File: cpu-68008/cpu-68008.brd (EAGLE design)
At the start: 96.8 x 100 mm, 65 parts, among them IC1 68008, IC11 NE555, IC2 AS6C4008, IC3 39SF010, IC4 DS1244Y, IC5 XR68C681, Q1 8MHz, Q3 3.6864 MHz

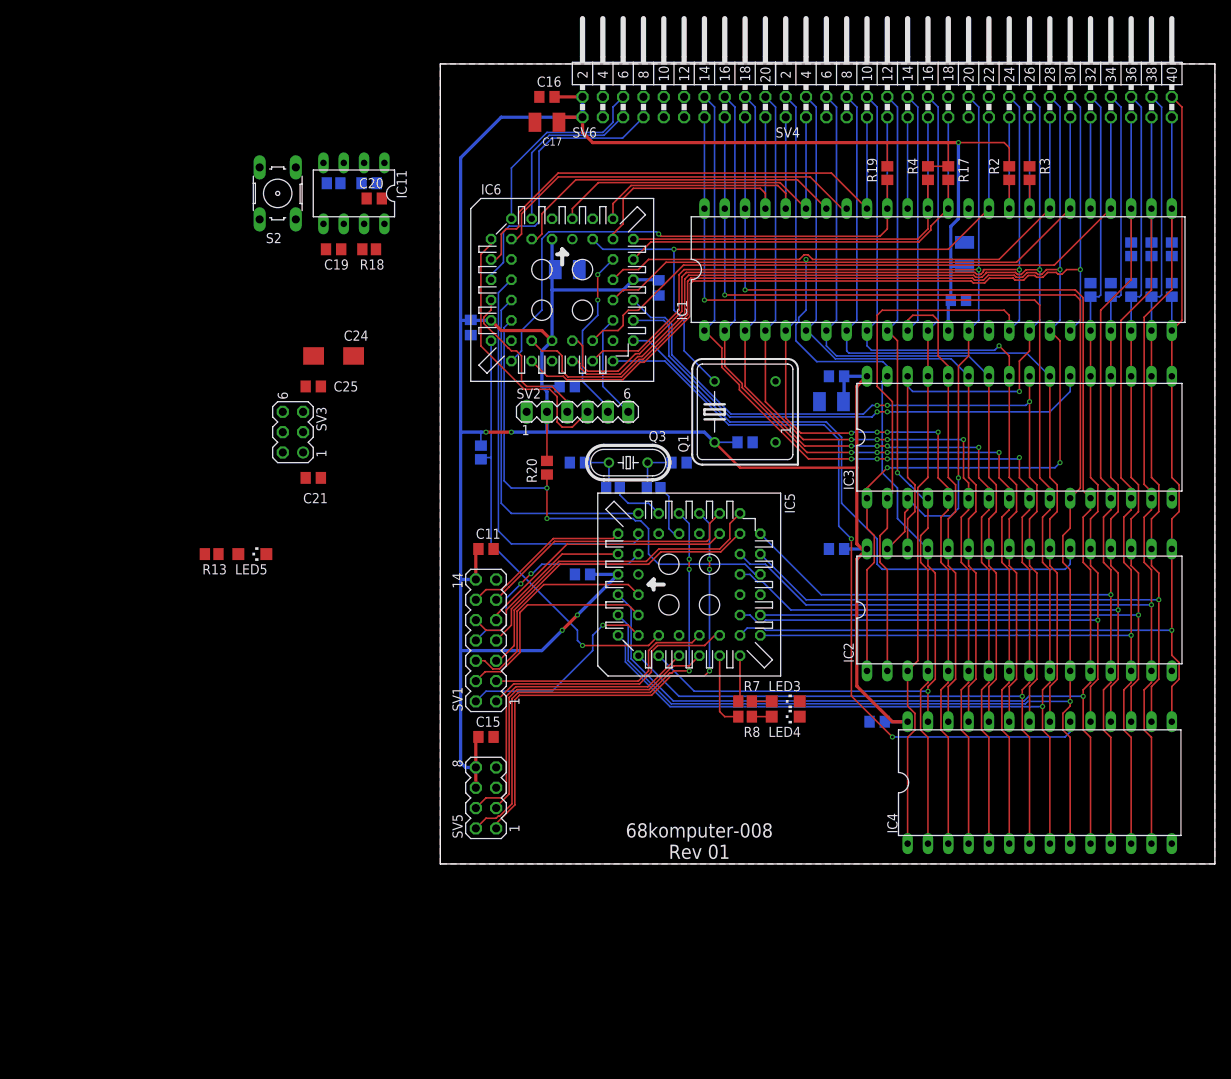
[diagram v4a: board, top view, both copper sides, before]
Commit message: finish routng
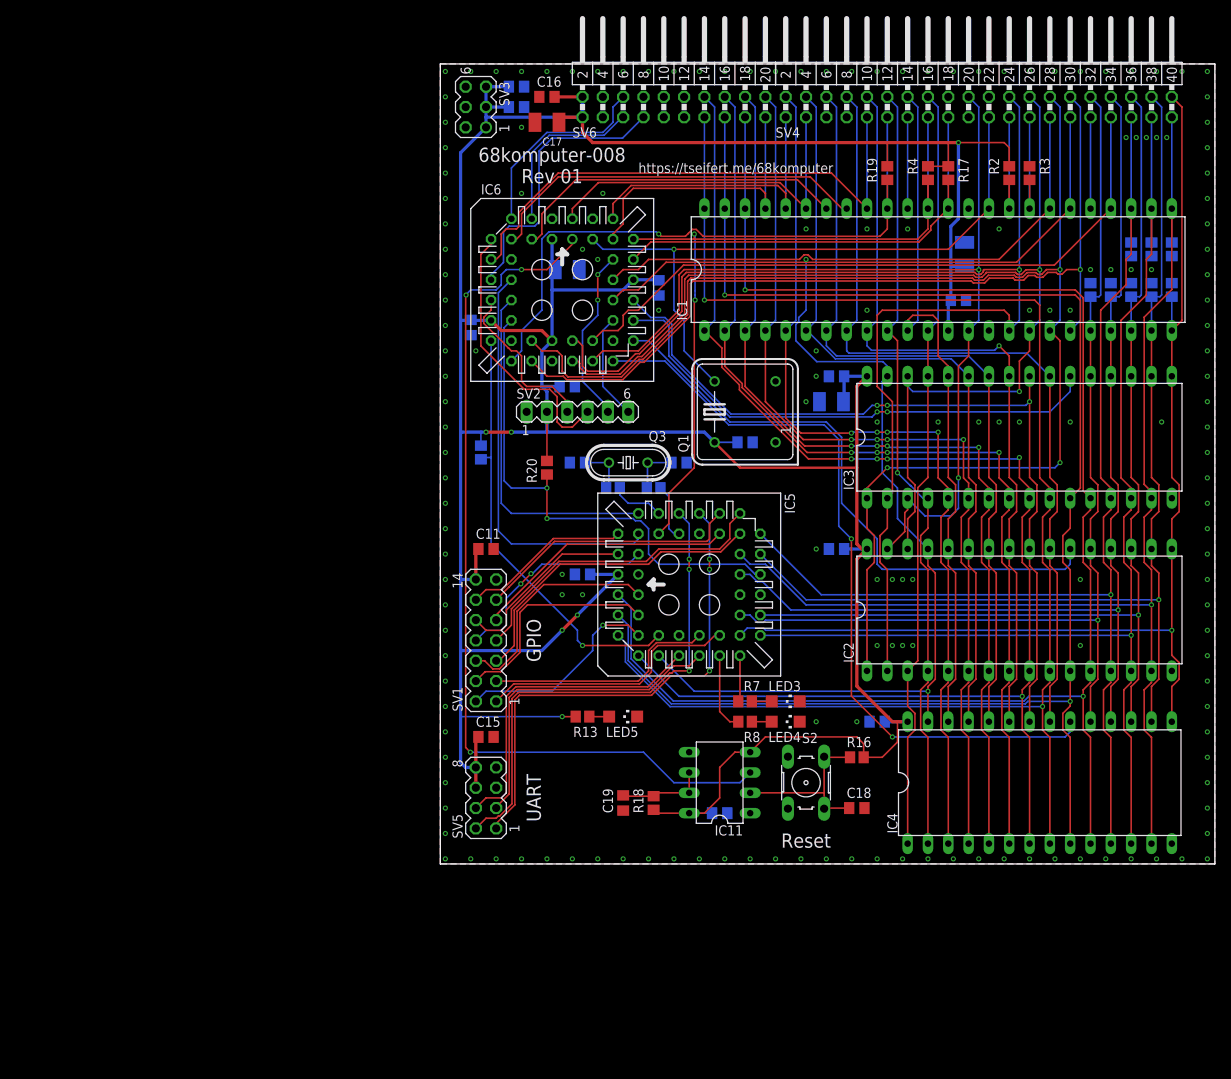
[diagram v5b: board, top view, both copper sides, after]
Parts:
- removed C24: 47µF, rcl:CT6032
- moved C18 99.1 mm to (52.1, 6.99), flipped to the top, turned to 0 degrees
- moved S2 98.9 mm to (45.7, 10.2), turned to 270 degrees
- moved R16 97.1 mm to (52.1, 13.3), flipped to the top
- moved C20 88.1 mm to (34.9, 6.35), flipped to the bottom
- moved IC11 86.7 mm to (34.9, 10.2), turned to 90 degrees
- moved C19 78.1 mm to (22.9, 7.62), turned to 270 degrees
- moved R18 77.8 mm to (26.7, 7.62), turned to 90 degrees
- moved C21 52.9 mm to (9.53, 94.6), flipped to the bottom, turned to 180 degrees
- moved LED5 50.6 mm to (22.9, 18.4)
- moved R13 50.6 mm to (17.8, 18.4)
- moved SV3 46.6 mm to (4.45, 94.6)
- moved C25 45.3 mm to (9.53, 97.2), flipped to the bottom, turned to 180 degrees
- moved LED4 0.63 mm to (43.2, 17.8)
- moved R8 0.63 mm to (38.1, 17.8)
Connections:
- net +5V: no longer C24.+
- net GND: no longer C24.-
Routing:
- net RESET: track 0.00 -> 111.8 mm, vias 0 -> 3
- net +5V: track 413.4 -> 483.5 mm, vias 5 -> 6
- net !RESET: track 54.9 -> 94.9 mm, vias 0 -> 2
- net N$1: track 0.00 -> 22.2 mm
- net N$12: track 0.00 -> 11.0 mm
- net N$4: track 0.00 -> 2.48 mm
- net !VPA: track 78.6 -> 79.3 mm
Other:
- board text added: "GPIO"
- board text added: "Reset"
- board text added: "UART"
- board text added: "https://tseifert.me/68komputer"

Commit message: a few routing improvements
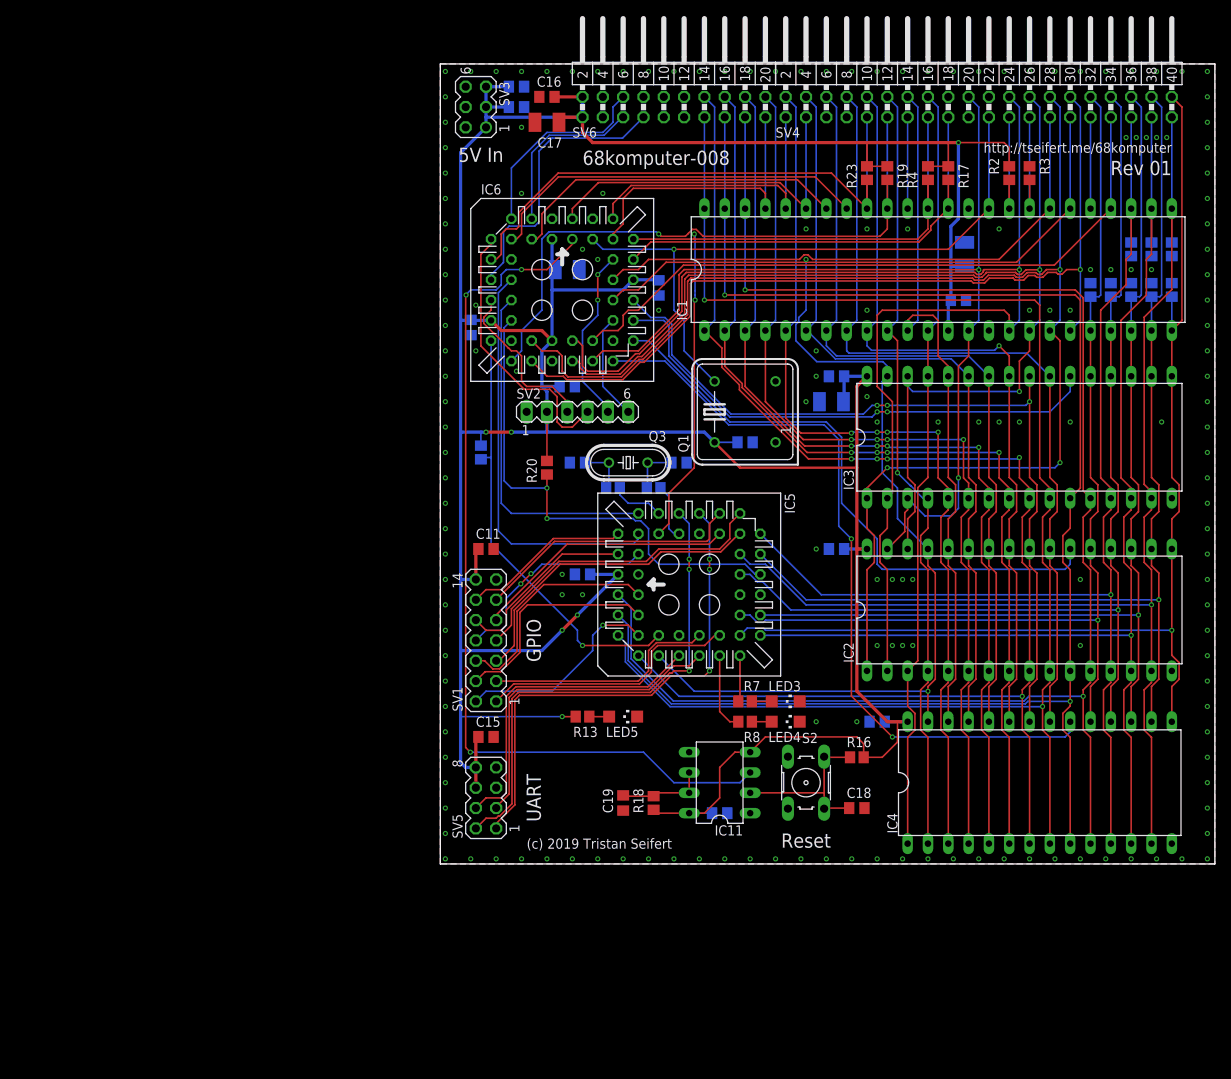
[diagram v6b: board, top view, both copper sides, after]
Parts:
- added R23: 10k, rcl:R2012
- IC6: value (none) -> ATF1504AS
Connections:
- net !BERR: now also R23.2
- net +5V: now also R23.1
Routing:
- net !BERR: track 67.3 -> 70.9 mm
- net +5V: track 483.5 -> 486.3 mm
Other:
- board text added: "(c) 2019 Tristan Seifert"
- board text added: "5V In"
- board text added: "68komputer-008"
- board text added: "Rev 01"
- board text added: "http://tseifert.me/68komputer"
- board text removed: "68komputer-008 Rev 01"
- board text removed: "https://tseifert.me/68komputer"

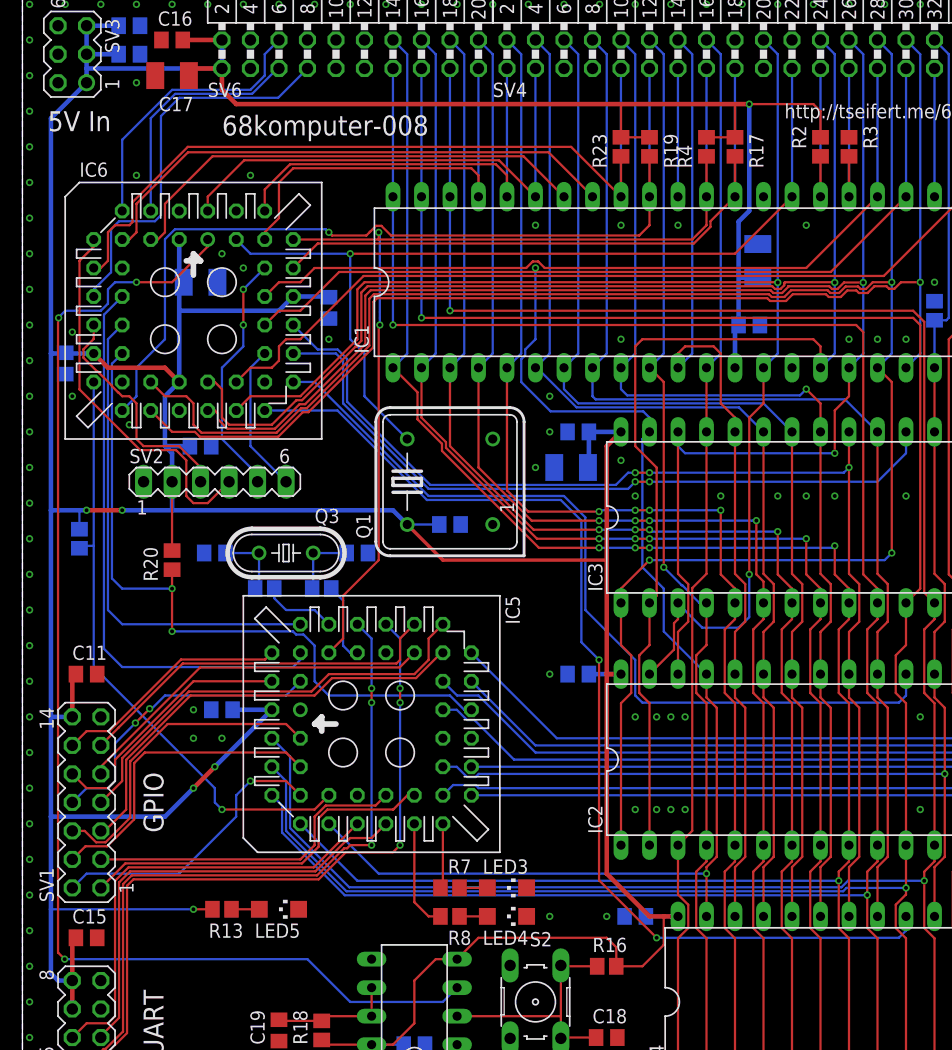
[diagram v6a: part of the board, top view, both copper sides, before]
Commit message: replaced CPLD with PLDs
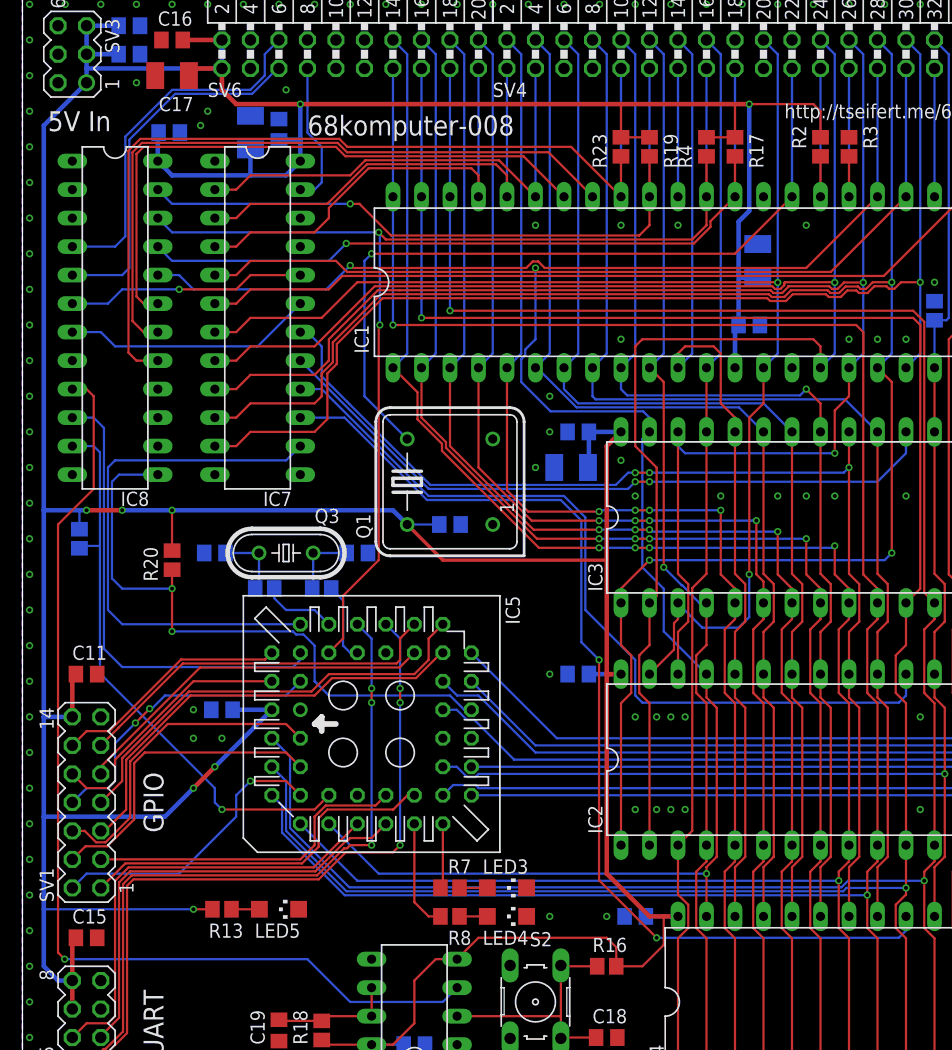
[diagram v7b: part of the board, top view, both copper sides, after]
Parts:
- removed C22: 100nF, rcl:C0805
- removed IC6: ATF1504AS, 68komputer:PLCC-S44
- removed SV2: (no value), con-lstb:MA06-1
- added IC7, IC8: (no value), 68komputer:DIL24S
- moved C9 28.2 mm to (22.9, 87.9), turned to 90 degrees
- moved C12 21.1 mm to (13.1, 87.6), turned to 180 degrees
- moved C14 14.1 mm to (20.3, 87.6), turned to 90 degrees
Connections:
- removed net CPLD_TCK: IC6.32, SV2.6
- removed net CPLD_TDI: IC6.7, SV2.4
- removed net CPLD_TDO: IC6.38, SV2.5
- removed net CPLD_TMS: IC6.13, SV2.3
- new net !IACK: IC7.19, IC8.7
- new net !REQUIRE_DTACK: IC7.20, IC8.6
- net !68681_CS: now also IC7.14; no longer IC6.14
- net !68681_DTACK: now also IC8.11; no longer IC6.17
- net !68681_IACK: now also IC8.10; no longer IC6.12
- net !68681_IRQ: now also IC8.13; no longer IC6.16
- net !AS: now also IC7.6; no longer IC6.27
- net !BERR: now also IC8.17; no longer IC6.9
- net !BUS_CS: now also IC7.23; no longer IC6.11
- net !BUS_DTACK: now also IC8.4; no longer IC6.6
- net !BUS_IRQ: now also IC8.5; no longer IC6.4
- net !DTACK: now also IC8.20; no longer IC6.36
- net !HALT: now also IC8.21; no longer IC6.37
- net !IPL0/2: now also IC8.19; no longer IC6.5
- net !IPL1: now also IC8.18; no longer IC6.8
- net !OE: now also IC7.18; no longer IC6.33
- net !RAM_CS: now also IC7.16; no longer IC6.29
- net !RESET: now also IC8.22; no longer IC6.39
- net !ROM_CS: now also IC7.17; no longer IC6.31
- net !RTC_CS: now also IC7.15; no longer IC6.28
- net !VPA: now also IC8.23; no longer IC6.18
- net +5V: now also IC7.24, IC8.24; no longer C22.1, IC6.15, IC6.23, IC6.3, IC6.35, SV2.2
- net A15: now also IC7.7; no longer IC6.26
- net A16: now also IC7.8; no longer IC6.25
- net A17: now also IC7.9; no longer IC6.24
- net A18: now also IC7.10; no longer IC6.21
- net A19: now also IC7.11; no longer IC6.20
- net CLK: no longer IC6.43
- net FC0: now also IC7.4; no longer IC6.41
- net FC1: now also IC7.3; no longer IC6.40
- net FC2: now also IC7.2; no longer IC6.44
- net GND: now also IC7.12, IC8.12; no longer C22.2, IC6.10, IC6.22, IC6.30, IC6.42, SV2.1
- net R/!W!: now also IC7.5; no longer IC6.34
- net RESET: now also IC8.9; no longer IC6.1
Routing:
- net CPLD_TDI: track 34.1 -> 0.00 mm
- net +5V: track 486.3 -> 458.4 mm, vias 6 -> 8
- net !IACK: track 0.00 -> 22.4 mm
- net !BUS_CS: track 35.2 -> 12.9 mm
- net CPLD_TDO: track 21.9 -> 0.00 mm, vias 2 -> 0
- net !REQUIRE_DTACK: track 0.00 -> 21.4 mm, vias 0 -> 1
- net CPLD_TMS: track 20.9 -> 0.00 mm
- net RESET: track 111.8 -> 91.0 mm, vias 3 -> 1
- net !VPA: track 79.3 -> 63.5 mm
- net CPLD_TCK: track 13.3 -> 0.00 mm
- net CLK: track 82.2 -> 69.4 mm
- net !IPL1: track 48.3 -> 61.1 mm
- net !HALT: track 57.3 -> 69.6 mm, vias 0 -> 1
- net !RESET: track 94.9 -> 107.2 mm
- net !IPL0/2: track 42.9 -> 55.1 mm
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
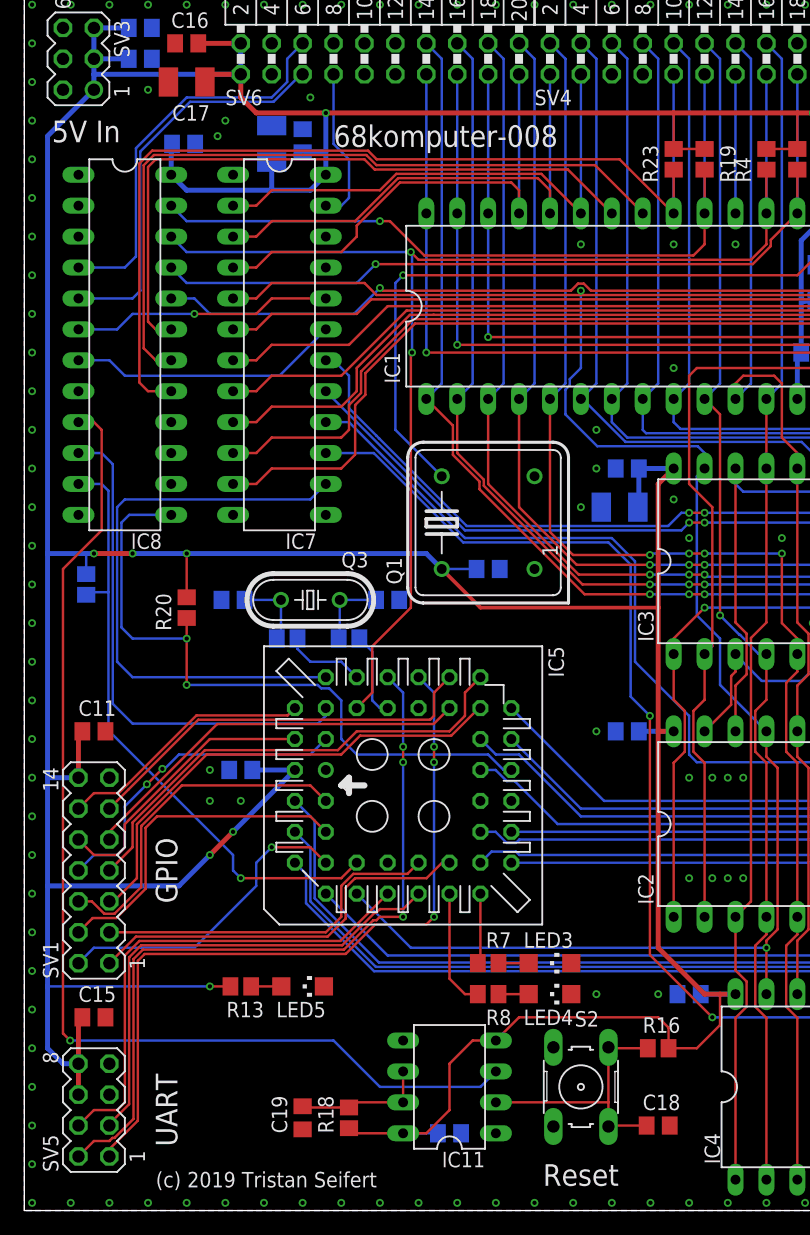
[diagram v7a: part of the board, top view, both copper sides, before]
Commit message: added bus error timeout circuit
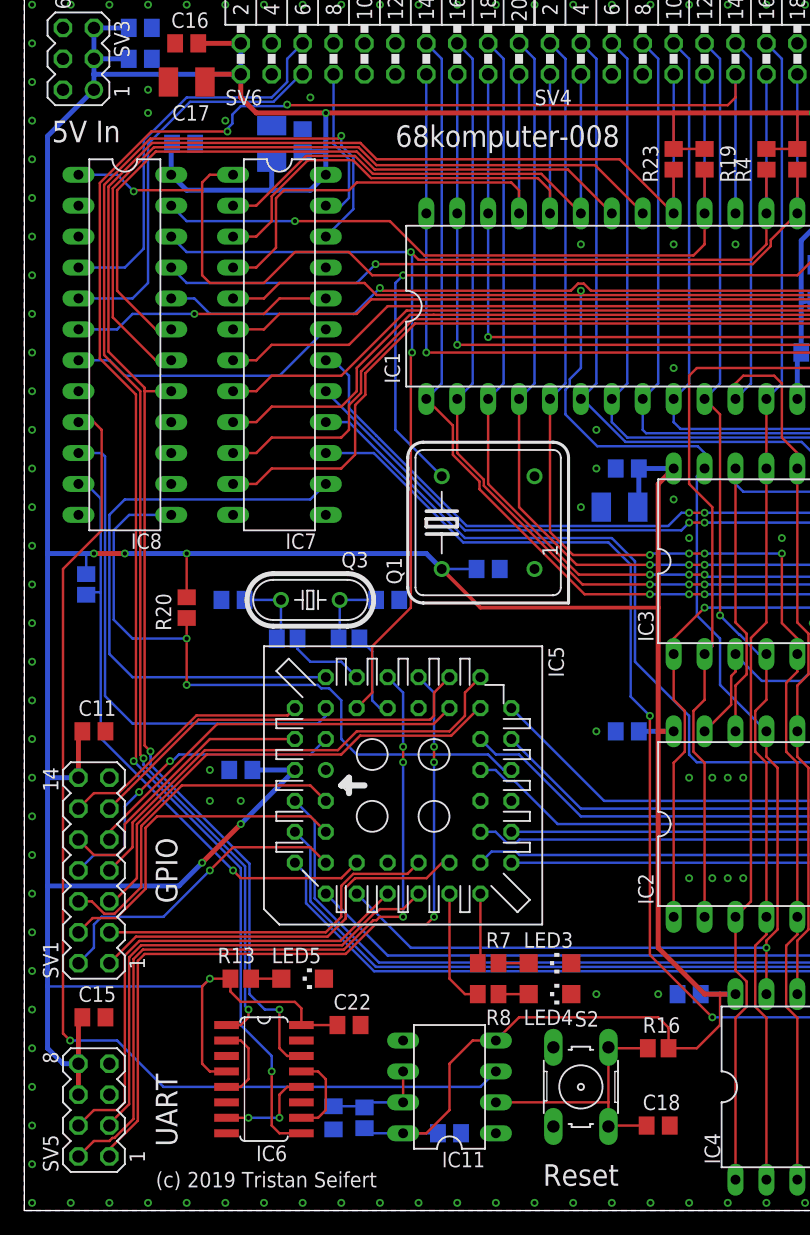
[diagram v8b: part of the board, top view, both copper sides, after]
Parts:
- added C22: 100nF, rcl:C0805
- added IC6: 74HC175D, 74xx-eu:SO16
- moved C19 2.54 mm to (25.4, 7.62), flipped to the bottom
- moved R18 1.27 mm to (27.9, 7.62), flipped to the bottom
- moved LED5 0.64 mm to (22.9, 19.1)
- moved R13 0.64 mm to (17.8, 19.1)
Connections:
- new net !BERR_TIMER_CLR: IC6.1, IC7.22
- new net N$5: IC6.2, IC6.5
- new net N$6: IC6.12, IC6.7
- new net N$8: IC6.10, IC6.13
- net !BERR: now also IC6.14
- net +5V: now also C22.1, IC6.16, IC6.4
- net CLK: now also IC7.1, IC8.1
- net E: now also IC6.9
- net GND: now also C22.2, IC6.8, IC7.13, IC8.2, IC8.3, IC8.8
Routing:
- net E: track 11.4 -> 155.2 mm, vias 0 -> 4
- net !BERR_TIMER_CLR: track 0.00 -> 106.1 mm, vias 0 -> 3
- net !BERR: track 82.4 -> 146.9 mm, vias 0 -> 2
- net CLK: track 69.4 -> 109.2 mm, vias 1 -> 2
- net +5V: track 458.4 -> 478.7 mm
- net N$6: track 0.00 -> 8.31 mm, vias 0 -> 2
- net N$8: track 0.00 -> 7.08 mm
- net N$5: track 0.00 -> 6.67 mm
- net !IPL1: track 61.1 -> 64.1 mm
- net !IPL0/2: track 55.1 -> 58.1 mm
- net N$12: track 11.0 -> 8.47 mm
- net FC1: track 41.8 -> 44.2 mm
- net FC0: track 40.5 -> 42.4 mm
- net !68681_DTACK: track 51.0 -> 49.6 mm
- net FC2: track 42.4 -> 43.7 mm
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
